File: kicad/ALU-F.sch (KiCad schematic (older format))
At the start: 31 parts, among them U21 74LS04, U22 74LS02, U23 74LS08, U24 74LS02, U25 74LS02, U26 74LS08, U27 74LS02, U28 74LS08, U29 74LS86, U30 74LS86, U31 74LS86, U32 74LS86, U33 74LS86, U34 74LS86, U35 74LS86

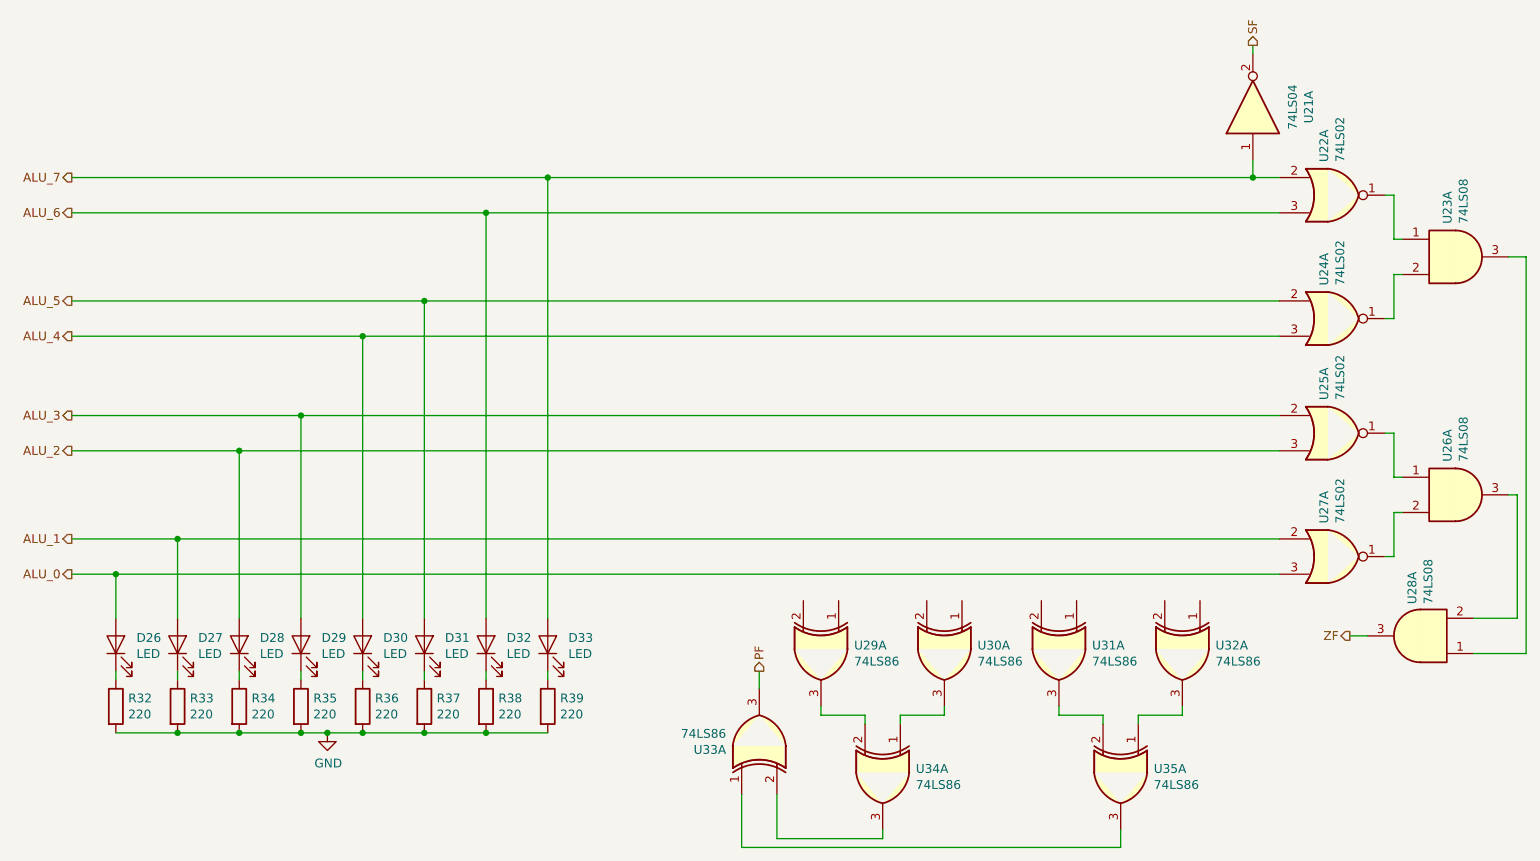
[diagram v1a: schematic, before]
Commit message: Reorganize part references
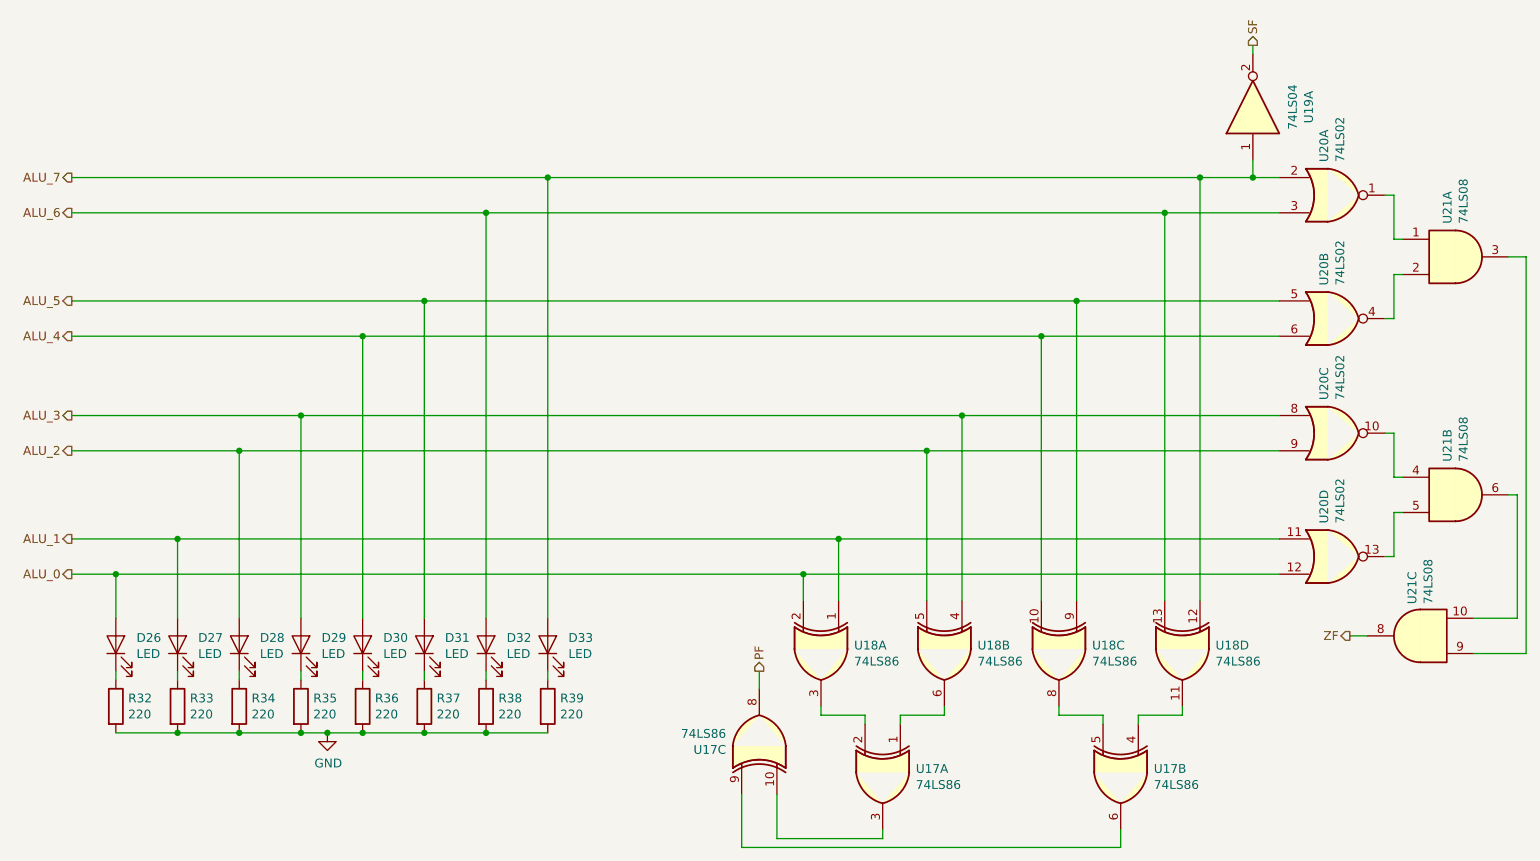
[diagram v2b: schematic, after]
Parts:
- renumbered U34 to U17, U35 to U17, U33 to U17, U29 to U18, U30 to U18, U31 to U18, U32 to U18, U21 to U19, U22 to U20, U24 to U20, U25 to U20, U27 to U20, U26 to U21, U23 to U21, U28 to U21
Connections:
- net ALU_0: now also U18.2, U20.12; no longer U20.3
- net ALU_1: now also U18.1, U20.11; no longer U20.2
- net ALU_2: now also U18.5, U20.9; no longer U20.3
- net ALU_3: now also U18.4, U20.8; no longer U20.2
- net ALU_4: now also U18.10, U20.6; no longer U20.3
- net ALU_5: now also U18.9, U20.5; no longer U20.2
- net ALU_6: now also U18.13
- net ALU_7: now also U18.12
- net PF: now also U17.8; no longer U17.3
- net ZF: now also U21.8; no longer U21.3
- net at U21.2: now also U20.4; no longer U20.1
- net at U21.3: now also U21.9; no longer U21.1
- net at U17.1: now also U18.6; no longer U18.3
- net at U17.3: now also U17.10; no longer U17.2
- new net: U20.10, U21.4
- new net: U20.13, U21.5
- new net: U21.10, U21.6
- new net: U17.5, U18.8
- new net: U17.4, U18.11
- new net: U17.6, U17.9
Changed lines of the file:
@@
 $Descr A4 11693 8268
 encoding utf-8
-Sheet 24 26
+Sheet 7 26
 Title ""
 Date "2019-10-03"
@@
 P 7850 1700
 AR Path="/5E5B2E62/5DE1A41C" Ref="U?"  Part="1"
-AR Path="/5E5B2E62/5DDD70EE/5DE1A41C" Ref="U21"  Part="1"
-F 0 "U21" H 7850 1383 50  0000 C CNN
+AR Path="/5E5B2E62/5DDD70EE/5DE1A41C" Ref="U19"  Part="1"
+F 0 "U19" H 7850 1383 50  0000 C CNN
 F 1 "74LS04" H 7850 1474 50  0000 C CNN
 F 2 "" H 7850 1700 50  0001 C CNN
@@
 P 8300 2200
 AR Path="/5E5B2E62/5DE74E09" Ref="U?"  Part="1"
-AR Path="/5E5B2E62/5DDD70EE/5DE74E09" Ref="U22"  Part="1"
-F 0 "U22" V 8254 2388 50  0000 L CNN
+AR Path="/5E5B2E62/5DDD70EE/5DE74E09" Ref="U20"  Part="1"
+F 0 "U20" V 8254 2388 50  0000 L CNN
 F 1 "74LS02" V 8345 2388 50  0000 L CNN
 F 2 "" H 8300 2200 50  0001 C CNN
@@
 $Comp
 L 74xx:74LS02 U?
-U 1 1 5DE74E0F
+U 2 1 5DE74E0F
 P 8300 2900
 AR Path="/5E5B2E62/5DE74E0F" Ref="U?"  Part="1"
-AR Path="/5E5B2E62/5DDD70EE/5DE74E0F" Ref="U24"  Part="1"
-F 0 "U24" V 8254 3088 50  0000 L CNN
+AR Path="/5E5B2E62/5DDD70EE/5DE74E0F" Ref="U20"  Part="2"
+F 0 "U20" V 8254 3088 50  0000 L CNN
 F 1 "74LS02" V 8345 3088 50  0000 L CNN
 F 2 "" H 8300 2900 50  0001 C CNN
 F 3 "http://www.ti.com/lit/gpn/sn74ls02" H 8300 2900 50  0001 C CNN
-	1    8300 2900
+	2    8300 2900
 	1    0    0    -1
 $EndComp
 $Comp
 L 74xx:74LS02 U?
-U 1 1 5DE74E15
+U 3 1 5DE74E15
 P 8300 3550
 AR Path="/5E5B2E62/5DE74E15" Ref="U?"  Part="1"
-AR Path="/5E5B2E62/5DDD70EE/5DE74E15" Ref="U25"  Part="1"
-F 0 "U25" V 8254 3738 50  0000 L CNN
+AR Path="/5E5B2E62/5DDD70EE/5DE74E15" Ref="U20"  Part="3"
+F 0 "U20" V 8254 3738 50  0000 L CNN
 F 1 "74LS02" V 8345 3738 50  0000 L CNN
 F 2 "" H 8300 3550 50  0001 C CNN
 F 3 "http://www.ti.com/lit/gpn/sn74ls02" H 8300 3550 50  0001 C CNN
-	1    8300 3550
+	3    8300 3550
 	1    0    0    -1
 $EndComp
 $Comp
 L 74xx:74LS02 U?
-U 1 1 5DE74E1B
+U 4 1 5DE74E1B
 P 8300 4250
 AR Path="/5E5B2E62/5DE74E1B" Ref="U?"  Part="1"
-AR Path="/5E5B2E62/5DDD70EE/5DE74E1B" Ref="U27"  Part="1"
-F 0 "U27" V 8254 4438 50  0000 L CNN
+AR Path="/5E5B2E62/5DDD70EE/5DE74E1B" Ref="U20"  Part="4"
+F 0 "U20" V 8254 4438 50  0000 L CNN
 F 1 "74LS02" V 8345 4438 50  0000 L CNN
 F 2 "" H 8300 4250 50  0001 C CNN
 F 3 "http://www.ti.com/lit/gpn/sn74ls02" H 8300 4250 50  0001 C CNN
-	1    8300 4250
+	4    8300 4250
 	1    0    0    -1
 $EndComp
 $Comp
 L 74xx:74LS08 U?
-U 1 1 5DE74E21
+U 2 1 5DE74E21
 P 9000 3900
 AR Path="/5E5B2E62/5DE74E21" Ref="U?"  Part="1"
-AR Path="/5E5B2E62/5DDD70EE/5DE74E21" Ref="U26"  Part="1"
-F 0 "U26" V 8954 4088 50  0000 L CNN
+AR Path="/5E5B2E62/5DDD70EE/5DE74E21" Ref="U21"  Part="2"
+F 0 "U21" V 8954 4088 50  0000 L CNN
 F 1 "74LS08" V 9045 4088 50  0000 L CNN
 F 2 "" H 9000 3900 50  0001 C CNN
 F 3 "http://www.ti.com/lit/gpn/sn74LS08" H 9000 3900 50  0001 C CNN
-	1    9000 3900
+	2    9000 3900
 	1    0    0    -1
 $EndComp
@@
 P 9000 2550
 AR Path="/5E5B2E62/5DE74E27" Ref="U?"  Part="1"
-AR Path="/5E5B2E62/5DDD70EE/5DE74E27" Ref="U23"  Part="1"
-F 0 "U23" V 8954 2738 50  0000 L CNN
+AR Path="/5E5B2E62/5DDD70EE/5DE74E27" Ref="U21"  Part="1"
+F 0 "U21" V 8954 2738 50  0000 L CNN
 F 1 "74LS08" V 9045 2738 50  0000 L CNN
 F 2 "" H 9000 2550 50  0001 C CNN
@@
 $Comp
 L 74xx:74LS08 U?
-U 1 1 5DE74E2D
+U 3 1 5DE74E2D
 P 8800 4700
 AR Path="/5E5B2E62/5DE74E2D" Ref="U?"  Part="1"
-AR Path="/5E5B2E62/5DDD70EE/5DE74E2D" Ref="U28"  Part="1"
-F 0 "U28" V 8846 4520 50  0000 R CNN
+AR Path="/5E5B2E62/5DDD70EE/5DE74E2D" Ref="U21"  Part="3"
+F 0 "U21" V 8846 4520 50  0000 R CNN
 F 1 "74LS08" V 8755 4520 50  0000 R CNN
 F 2 "" H 8800 4700 50  0001 C CNN
 F 3 "http://www.ti.com/lit/gpn/sn74LS08" H 8800 4700 50  0001 C CNN
-	1    8800 4700
+	3    8800 4700
 	-1   0    0    1
 $EndComp
@@
 	9400 2550 9400 4800
 Wire Wire Line
-	8000 4350 1400 4350
-Wire Wire Line
 	1150 4150 1750 4150
 Wire Wire Line
-	8000 3650 2100 3650
+	8000 3650 6000 3650
 Wire Wire Line
 	1150 3450 2450 3450
 Wire Wire Line
-	8000 3000 2800 3000
-Wire Wire Line
-	8000 2800 3150 2800
+	8000 3000 6650 3000
+Wire Wire Line
+	8000 2800 6850 2800
 Wire Wire Line
 	1150 2100 3850 2100
@@
 Connection ~ 1750 4150
 Wire Wire Line
-	1750 4150 8000 4150
+	1750 4150 5500 4150
 Wire Wire Line
 	2100 4600 2100 3650
@@
 Connection ~ 2450 3450
 Wire Wire Line
-	2450 3450 8000 3450
+	2450 3450 6200 3450
 Wire Wire Line
 	2800 3000 2800 4600
@@
 Connection ~ 3500 2300
 Wire Wire Line
-	3500 2300 8000 2300
+	3500 2300 7350 2300
 Wire Wire Line
 	3850 2100 3850 4600
 Connection ~ 3850 2100
 Wire Wire Line
-	3850 2100 7850 2100
+	3850 2100 7550 2100
 Wire Wire Line
 	5050 4900 5050 5000
@@
 	7100 5900 4950 5900
 $Comp
-L 74xx:74LS86 U29
+L 74xx:74LS86 U18
 U 1 1 5E39691C
 P 5400 4800
-F 0 "U29" V 5354 4988 50  0000 L CNN
+F 0 "U18" V 5354 4988 50  0000 L CNN
 F 1 "74LS86" V 5445 4988 50  0000 L CNN
 F 2 "" H 5400 4800 50  0001 C CNN
@@
 $EndComp
 $Comp
-L 74xx:74LS86 U30
-U 1 1 5E39C36C
+L 74xx:74LS86 U18
+U 2 1 5E39C36C
 P 6100 4800
-F 0 "U30" V 6054 4988 50  0000 L CNN
+F 0 "U18" V 6054 4988 50  0000 L CNN
 F 1 "74LS86" V 6145 4988 50  0000 L CNN
 F 2 "" H 6100 4800 50  0001 C CNN
 F 3 "74xx/74ls86.pdf" H 6100 4800 50  0001 C CNN
-	1    6100 4800
+	2    6100 4800
 	0    1    1    0
 $EndComp
 $Comp
-L 74xx:74LS86 U31
-U 1 1 5E44ADC0
+L 74xx:74LS86 U18
+U 3 1 5E44ADC0
 P 6750 4800
-F 0 "U31" V 6704 4988 50  0000 L CNN
+F 0 "U18" V 6704 4988 50  0000 L CNN
 F 1 "74LS86" V 6795 4988 50  0000 L CNN
 F 2 "" H 6750 4800 50  0001 C CNN
 F 3 "74xx/74ls86.pdf" H 6750 4800 50  0001 C CNN
-	1    6750 4800
+	3    6750 4800
 	0    1    1    0
 $EndComp
 $Comp
-L 74xx:74LS86 U32
-U 1 1 5E44ADC6
+L 74xx:74LS86 U18
+U 4 1 5E44ADC6
 P 7450 4800
-F 0 "U32" V 7404 4988 50  0000 L CNN
+F 0 "U18" V 7404 4988 50  0000 L CNN
 F 1 "74LS86" V 7495 4988 50  0000 L CNN
 F 2 "" H 7450 4800 50  0001 C CNN
 F 3 "74xx/74ls86.pdf" H 7450 4800 50  0001 C CNN
-	1    7450 4800
+	4    7450 4800
 	0    1    1    0
 $EndComp
 $Comp
-L 74xx:74LS86 U34
+L 74xx:74LS86 U17
 U 1 1 5E44EC9C
 P 5750 5500
-F 0 "U34" V 5704 5688 50  0000 L CNN
+F 0 "U17" V 5704 5688 50  0000 L CNN
 F 1 "74LS86" V 5795 5688 50  0000 L CNN
 F 2 "" H 5750 5500 50  0001 C CNN
@@
 $EndComp
 $Comp
-L 74xx:74LS86 U35
-U 1 1 5E44ECA2
+L 74xx:74LS86 U17
+U 2 1 5E44ECA2
 P 7100 5500
-F 0 "U35" V 7054 5688 50  0000 L CNN
+F 0 "U17" V 7054 5688 50  0000 L CNN
 F 1 "74LS86" V 7145 5688 50  0000 L CNN
 F 2 "" H 7100 5500 50  0001 C CNN
 F 3 "74xx/74ls86.pdf" H 7100 5500 50  0001 C CNN
-	1    7100 5500
+	2    7100 5500
 	0    1    1    0
 $EndComp
 $Comp
-L 74xx:74LS86 U33
-U 1 1 5E464A29
+L 74xx:74LS86 U17
+U 3 1 5E464A29
 P 5050 5300
-F 0 "U33" V 5004 5488 50  0000 L CNN
+F 0 "U17" V 5004 5488 50  0000 L CNN
 F 1 "74LS86" V 5095 5488 50  0000 L CNN
 F 2 "" H 5050 5300 50  0001 C CNN
 F 3 "74xx/74ls86.pdf" H 5050 5300 50  0001 C CNN
-	1    5050 5300
-	0    -1   -1   0
-$EndComp
+	3    5050 5300
+	0    -1   -1   0
+$EndComp
+Wire Wire Line
+	8000 4350 5300 4350
+Wire Wire Line
+	5300 4500 5300 4350
+Connection ~ 5300 4350
+Wire Wire Line
+	5300 4350 1400 4350
+Wire Wire Line
+	5500 4500 5500 4150
+Connection ~ 5500 4150
+Wire Wire Line
+	5500 4150 8000 4150
+Wire Wire Line
+	6000 4500 6000 3650
+Connection ~ 6000 3650
+Wire Wire Line
+	6000 3650 2100 3650
+Wire Wire Line
+	6200 4500 6200 3450
+Connection ~ 6200 3450
+Wire Wire Line
+	6200 3450 8000 3450
+Wire Wire Line
+	6650 4500 6650 3000
+Connection ~ 6650 3000
+Wire Wire Line
+	6650 3000 2800 3000
+Wire Wire Line
+	6850 4500 6850 2800
+Connection ~ 6850 2800
+Wire Wire Line
+	6850 2800 3150 2800
+Wire Wire Line
+	7350 4500 7350 2300
+Connection ~ 7350 2300
+Wire Wire Line
+	7350 2300 8000 2300
+Wire Wire Line
+	7550 2100 7550 4500
+Connection ~ 7550 2100
+Wire Wire Line
+	7550 2100 7850 2100
 $EndSCHEMATC
